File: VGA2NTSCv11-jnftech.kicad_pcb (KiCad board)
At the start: 2 copper layers, 58.4 x 99.8 mm, 57 parts, among them J1 RCA Yellow, J3 MD-40SM, J4 SCART Female, J5 RCA White, J6 RCA Red, J7 Micro USB, U1 Video Buffer, U2 Encoder, U3 OSC/DIV, X1 XTAL

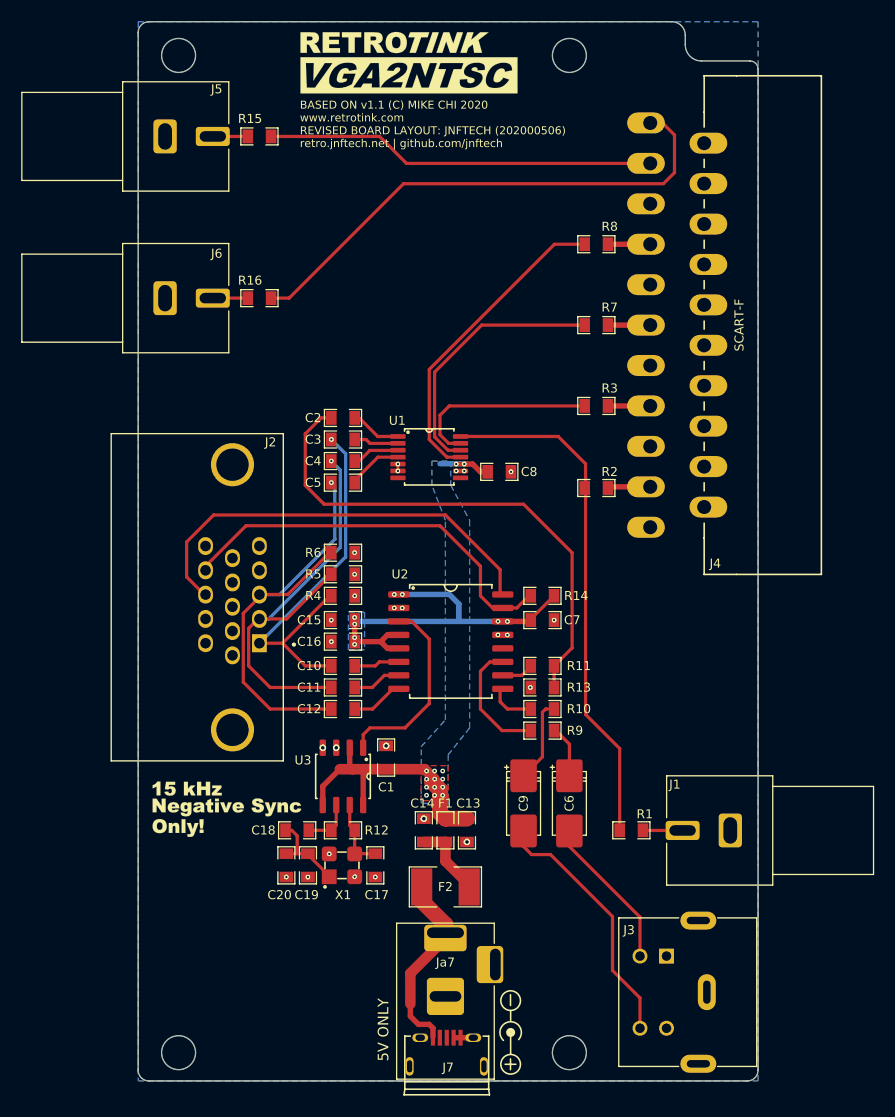
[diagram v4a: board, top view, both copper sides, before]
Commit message: Updating project to 20210703 version
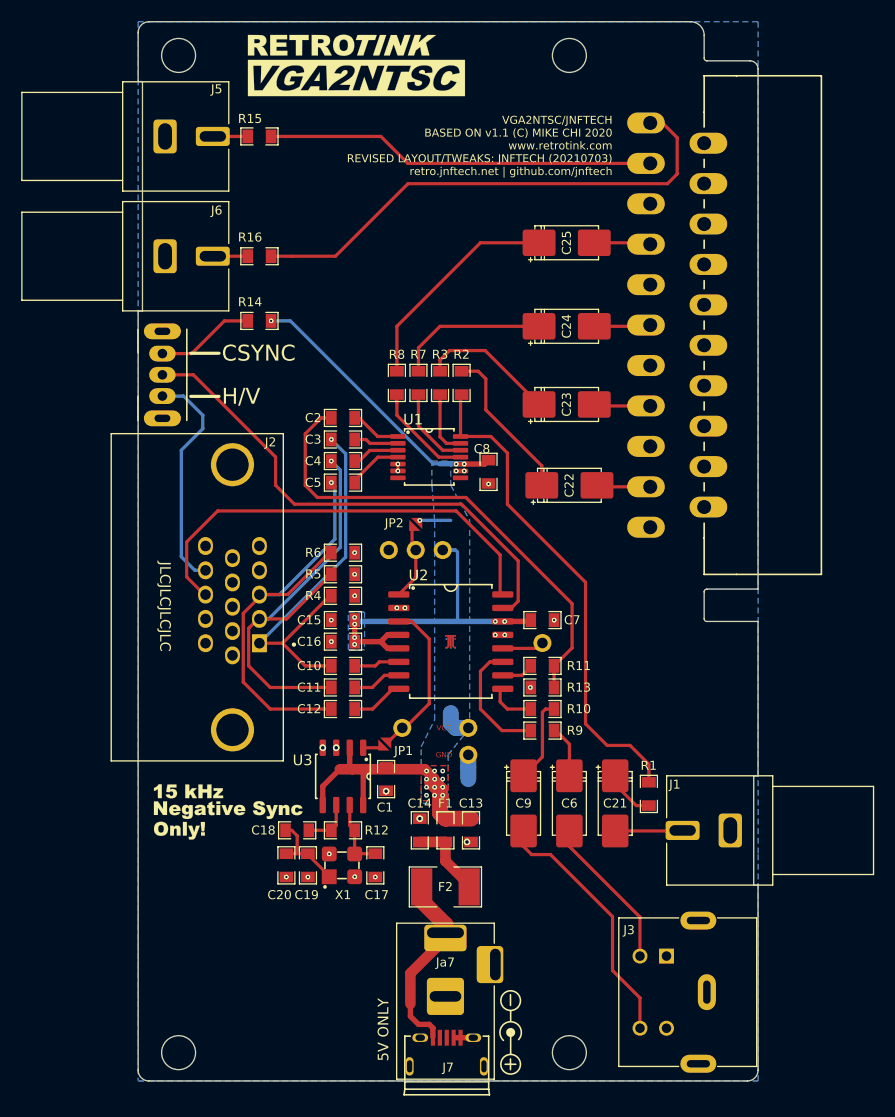
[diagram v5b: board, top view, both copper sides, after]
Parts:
- added C21: Cap 220uf Case C, VGA2NTSC:CP_Tantalum_Case-C_EIA-6032-28_JFT, F.Cu at (174.5, 97.3)
- added C22: Cap 220uf Case C, VGA2NTSC:CP_Tantalum_Case-C_EIA-6032-28_JFT, F.Cu at (170.2, 67.3)
- added C23: Cap 220uf Case C, VGA2NTSC:CP_Tantalum_Case-C_EIA-6032-28_JFT, F.Cu at (169.9, 59.7)
- added C24: Cap 220uf Case C, VGA2NTSC:CP_Tantalum_Case-C_EIA-6032-28_JFT, F.Cu at (169.9, 52.3)
- added C25: Cap 220uf Case C, VGA2NTSC:CP_Tantalum_Case-C_EIA-6032-28_JFT, F.Cu at (169.9, 44.5)
- added G***: LOGO, VGA2NTSC:JFTLOGO-1x1.3mm, B.Cu at (159.0, 82.0)
- added G***: LOGO, VGA2NTSC:JFTLOGO-1x1.3mm, F.Cu at (159.0, 82.0)
- added JP1: Jumper_NO_Small, VGA2NTSC:WirepadJumperSm, F.Cu at (152.8, 91.7)
- added JP2: Jumper_NO_Small, VGA2NTSC:WirepadJumperSm, F.Cu at (155.7, 71.0)
- added P1: EXT_CLOCK, VGA2NTSC:TH_Hole_One_1mm, F.Cu at (154.4, 90.2)
- added P2: EXT_STD_TOGGLE, VGA2NTSC:Pin_Header_Straight_1x03_Pitch2.54mm_NoSilk, F.Cu at (153.2, 73.4)
- added P3: YTRAP_FEED, VGA2NTSC:TH_Hole_One_1mm, F.Cu at (167.6, 82.2)
- added P4: VCC_TAP, VGA2NTSC:TH_Hole_One_1mm, F.Cu at (160.7, 90.2)
- added P5: GND_TAP, VGA2NTSC:TH_Hole_One_1mm, F.Cu at (160.7, 92.7)
- added SW1: SW_SPDT, VGA2NTSC:SW_HRO-SK-12D02_SPDT_Angled, F.Cu at (131.8, 56.9)
- C13, C14: value Cap 10uF 0603 -> 10uf
- C6, C9: value Cap 100uF 1210 -> Cap 220uf Case C
- J1, J5, J6: footprint VGA2NTSC:RCJ-04x -> VGA2NTSC:RCJ-04x_NoHole
- J4: footprint VGA2NTSC:SCART-F-RA-Pin11centerNPTH -> VGA2NTSC:SCART-F-RA-NoHole
- R11, R13: value Res 1k 0402 -> 1K
- R12: value Res 1M 0402 -> 1M
- R15, R16: value 49.9 -> 49R9
- moved R14 37.2 mm to (141.0, 51.8)
- moved R8 22.9 mm to (153.9, 57.7), turned to 90 degrees
- moved R7 17.6 mm to (156.0, 57.7), turned to 90 degrees
- moved R2 16.1 mm to (160.0, 57.7), turned to 90 degrees
- moved R3 14.9 mm to (158.0, 57.7), turned to 90 degrees
- moved G*** 4.96 mm to (150.2, 30.2)
- moved J6 3.95 mm to (132.1, 45.7)
- moved R16 3.95 mm to (141.0, 45.7)
- moved R1 3.81 mm to (177.7, 96.4), turned to 270 degrees
- moved C1 2.03 mm to (152.9, 95.0), turned to 90 degrees
- moved C8 1.02 mm to (162.6, 66.0), turned to 90 degrees
- moved C13 0.38 mm to (160.9, 99.8)
- moved C14 0.38 mm to (156.1, 99.8)
- moved G*** 0.28 mm to (138.0, 98.0)
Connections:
- J2 pad 14: /VS -> Net-(J2-Pad14)
- R1 pad 2: /CVBS_OUT -> Net-(C21-Pad1)
- R14 pad 2: /VS -> Net-(R14-Pad2)
- R2 pad 2: /CSYNC_OUT -> Net-(C22-Pad1)
- R3 pad 2: /ROUT -> Net-(C23-Pad1)
- R7 pad 2: /GOUT -> Net-(C24-Pad1)
- R8 pad 2: /BOUT -> Net-(C25-Pad1)
- U2 pad 1: VCC -> Net-(JP2-Pad1)
- U3 pad 1: /CLOCK -> Net-(JP1-Pad2)
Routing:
- net VCC: track 67.9 -> 91.6 mm
- net Net-(J2-Pad14): track 0.00 -> 21.9 mm
- net Net-(C25-Pad1): track 0.00 -> 20.9 mm
- net Net-(R8-Pad1): track 29.8 -> 9.58 mm
- net Net-(R7-Pad1): track 25.0 -> 7.88 mm
- net Net-(C24-Pad1): track 0.00 -> 14.9 mm
- net Net-(C22-Pad1): track 0.00 -> 14.8 mm
- net Net-(C23-Pad1): track 0.00 -> 13.4 mm
- net Net-(R3-Pad1): track 18.1 -> 6.17 mm
- net /VS: track 37.9 -> 48.1 mm
- net Net-(R14-Pad2): track 0.00 -> 9.32 mm
- net Net-(JP2-Pad1): track 0.00 -> 7.06 mm
- net Net-(C21-Pad1): track 0.00 -> 5.22 mm
- net Net-(P3-Pad1): track 0.00 -> 3.95 mm
- net /CLOCK: track 18.1 -> 14.7 mm
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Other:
- outline, holes or cut-outs redrawn
- board text added: "CSYNC"
- board text added: "EXT_OSC"
- board text added: "GND"
- board text added: "H/V"
- board text added: "JLCJLCJLCJLC"
- board text added: "JP1"
- board text added: "JP1: CLOSE FOR NORMAL NTSC MODE OPEN TO SUPPLY EXTERNAL OSC (INTO NEARBY PIN) JP2: CLOSE FOR NORMAL NTSC MODE OPEN TO USE NEARBY JUMPER PINS TO SELECT NTSC/PAL (MUST USE EXTERNAL OSC)"
- board text added: "NTSC"
- board text added: "PAL"
- board text added: "VCC"
- board text added: "VGA2NTSC/JNFTECH BASED ON v1.1 (C) MIKE CHI 2020 www.retrotink.com REVISED LAYOUT/TWEAKS: JNFTECH (20210703) retro.jnftech.net | github.com/jnftech"
- board text added: "YTRAP"
- board text removed: "BASED ON v1.1 (C) MIKE CHI 2020 www.retrotink.com REVISED BOARD LAYOUT: JNFTECH (202000506) retro.jnftech.net | github.com/jnftech"
- board text removed: "R2"
- board text removed: "R3"
- board text removed: "R7"
- board text removed: "R8"
- board text removed: "U1"
- board text removed: "U2"
- board text removed: "U3"
